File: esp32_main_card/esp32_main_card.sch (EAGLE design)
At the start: 4 parts, among them J1 09231486921, U3 ESP32-DEVKITC-32D

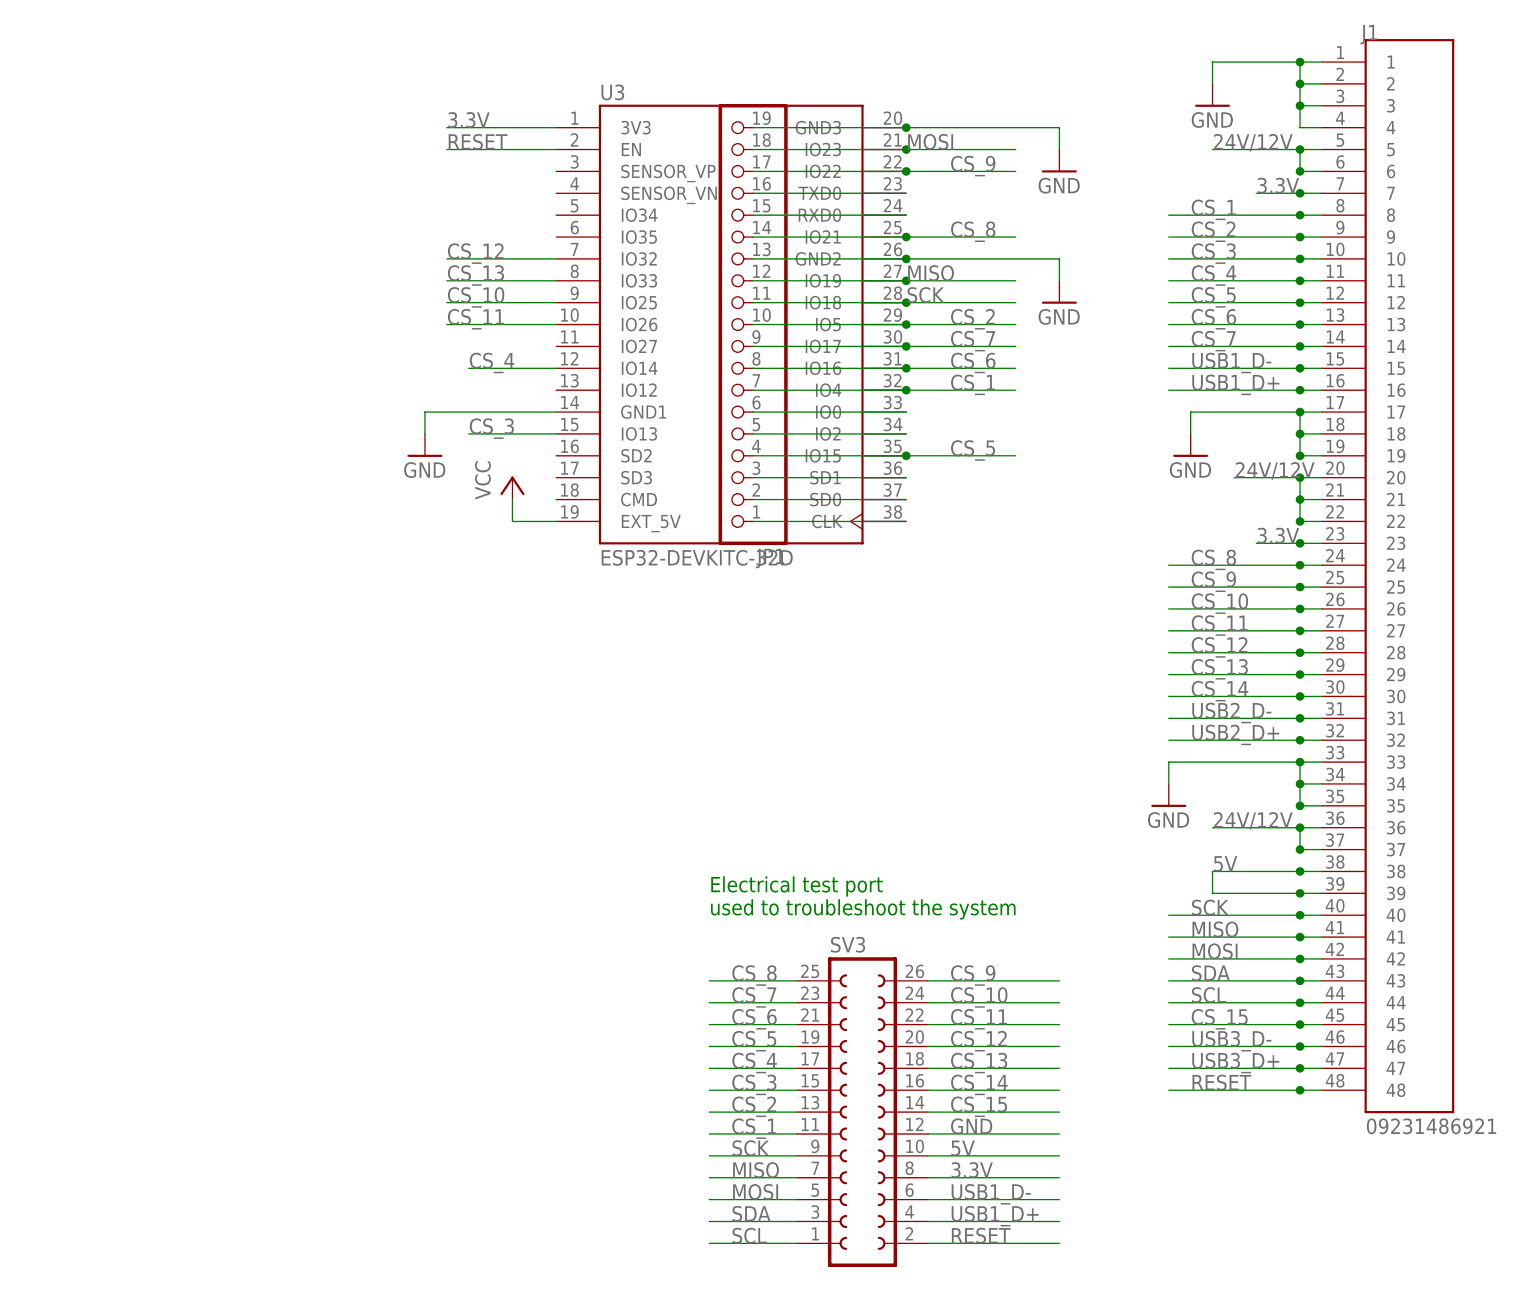
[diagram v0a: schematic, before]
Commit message: made card holes bigger, started usb port work, but I'm not done that part yet
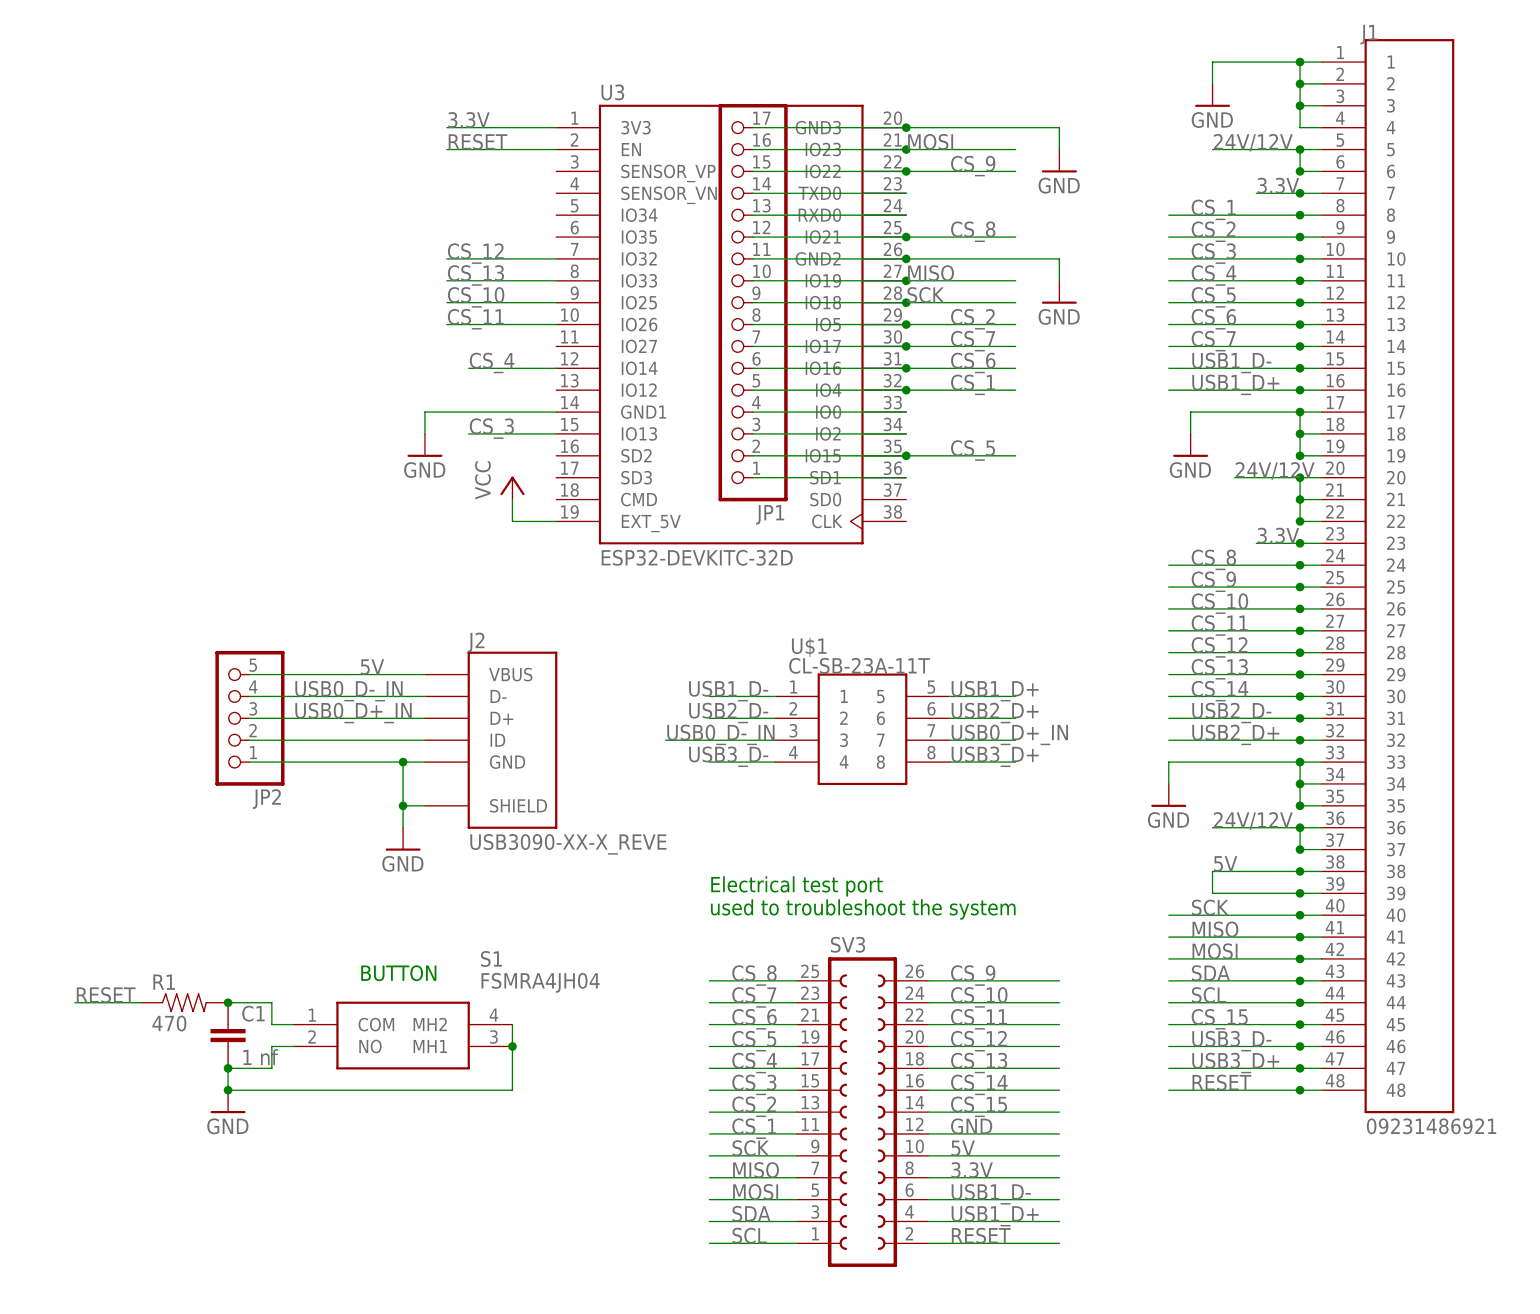
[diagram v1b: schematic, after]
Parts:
- added C1: 1 nf, SparkFun-Passives:CAP0805
- added J2: USB3090-XX-X_REVE, USB3090-XX-X_REVE:USB3090-XX-X_REVE
- added JP2: (no value), pinhead:PINHD-1X5
- added R1: 470, SparkFun-Passives:RESISTOR0805-RES
- added S1: FSMRA4JH04, FSMRA4JH04:FSMRA4JH04
- added U$1: CL-SB-23A-11T, CL-SB-23A-11T:CL-SB-23A-11T
- JP1: device pinhead:PINHD-1X19 -> pinhead:PINHD-1X17; COMPONENT female header 1x19 -> (none)
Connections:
- removed net N$9: JP1.1, U3.CLK
- new net N$1: J2.ID, JP2.2
- new net N$2: JP1.17, U3.GND3
- new net USB0_D+_IN: J2.D+, JP2.3, U$1.7
- new net USB0_D-_IN: J2.D-, JP2.4, U$1.3
- net 5V: now also J2.VBUS, JP2.5
- net CS_1: now also JP1.5; no longer JP1.7
- net CS_2: now also JP1.8; no longer JP1.10
- net CS_5: now also JP1.2; no longer JP1.4
- net CS_6: now also JP1.6; no longer JP1.8
- net CS_7: now also JP1.7; no longer JP1.9
- net CS_8: now also JP1.12; no longer JP1.14
- net CS_9: now also JP1.15; no longer JP1.17
- net GND: now also C1.2, J2.GND, J2.SHIELD, JP1.11, JP2.1, S1.MH1, S1.MH2, S1.NO; no longer JP1.13, JP1.19, U3.GND3
- net MISO: now also JP1.10; no longer JP1.12
- net MOSI: now also JP1.16; no longer JP1.18
- net N$3: now also JP1.14; no longer JP1.16
- net N$4: now also JP1.13; no longer JP1.15
- net N$5: now also JP1.4; no longer JP1.6
- net N$6: now also JP1.3; no longer JP1.5
- net N$7: now also JP1.1; no longer JP1.3
- net N$8: now also C1.1, R1.2, S1.COM; no longer JP1.2, U3.SD0
- net RESET: now also R1.1
- net SCK: now also JP1.9; no longer JP1.11
- net USB1_D+: now also U$1.5
- net USB1_D-: now also U$1.1
- net USB2_D+: now also U$1.6
- net USB2_D-: now also U$1.2
- net USB3_D+: now also U$1.8
- net USB3_D-: now also U$1.4
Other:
- note added: "BUTTON"

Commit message: added on light to main card
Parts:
- added LED1: (no value), led:LED3MM
- added R2: 180, SparkFun-Passives:RESISTOR0805-RES
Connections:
- net VCC renamed N$10
- new net N$9: LED1.C, R2.2
- net 3.3V: now also LED1.A
- net GND: now also R2.1
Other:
- note added: "ON light"
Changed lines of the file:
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@@
 <part name="GND3" library="supply1" library_urn="urn:adsk.eagle:library:371" deviceset="GND" device=""/>
 <part name="U3" library="ESP32-DEVKITC-32D" deviceset="ESP32-DEVKITC-32D" device=""/>
-<part name="P+4" library="supply1" library_urn="urn:adsk.eagle:library:371" deviceset="VCC" device=""/>
 <part name="GND9" library="supply1" library_urn="urn:adsk.eagle:library:371" deviceset="GND" device=""/>
 <part name="GND10" library="supply1" library_urn="urn:adsk.eagle:library:371" deviceset="GND" device=""/>
@@
 <part name="R1" library="SparkFun-Passives" deviceset="RESISTOR" device="0805-RES" package3d_urn="urn:adsk.eagle:package:30824479/1" value="470"/>
 <part name="GND5" library="supply1" library_urn="urn:adsk.eagle:library:371" deviceset="GND" device=""/>
+<part name="LED1" library="led" library_urn="urn:adsk.eagle:library:259" deviceset="LED" device="3MM" package3d_urn="urn:adsk.eagle:package:15797/1">
+<attribute name="COLOR" value="green"/>
+</part>
+<part name="R2" library="SparkFun-Passives" deviceset="RESISTOR" device="0805-RES" package3d_urn="urn:adsk.eagle:package:30824479/1" value="180"/>
+<part name="GND6" library="supply1" library_urn="urn:adsk.eagle:library:371" deviceset="GND" device=""/>
 </parts>
 <sheets>
@@
 used to troubleshoot the system</text>
 <text x="-55.88" y="0" size="1.778" layer="91">BUTTON</text>
+<text x="-93.98" y="63.5" size="1.778" layer="91">ON light</text>
 </plain>
 <instances>
@@
 <attribute name="VALUE" x="-27.9563" y="48.2302" size="1.7799" layer="96"/>
 </instance>
-<instance part="P+4" gate="VCC" x="-38.1" y="58.42" smashed="yes">
-<attribute name="VALUE" x="-40.64" y="55.88" size="1.778" layer="96" rot="R90"/>
-</instance>
 <instance part="GND9" gate="1" x="-48.26" y="60.96" smashed="yes">
 <attribute name="VALUE" x="-50.8" y="58.42" size="1.778" layer="96"/>
@@
 <instance part="GND5" gate="1" x="-71.12" y="-15.24" smashed="yes">
 <attribute name="VALUE" x="-73.66" y="-17.78" size="1.778" layer="96"/>
+</instance>
+<instance part="LED1" gate="G$1" x="-91.44" y="53.34" smashed="yes">
+<attribute name="NAME" x="-87.884" y="48.768" size="1.778" layer="95" rot="R90"/>
+<attribute name="VALUE" x="-85.725" y="48.768" size="1.778" layer="96" rot="R90"/>
+<attribute name="COLOR" x="-91.44" y="53.34" size="1.778" layer="96" display="off"/>
+</instance>
+<instance part="R2" gate="G$1" x="-91.44" y="43.18" smashed="yes" rot="R90">
+<attribute name="NAME" x="-92.9386" y="39.37" size="1.778" layer="95" rot="R90"/>
+<attribute name="VALUE" x="-88.138" y="39.37" size="1.778" layer="96" rot="R90"/>
+</instance>
+<instance part="GND6" gate="1" x="-91.44" y="35.56" smashed="yes">
+<attribute name="VALUE" x="-93.98" y="33.02" size="1.778" layer="96"/>
 </instance>
 </instances>
@@
 <junction x="-71.12" y="-12.7"/>
 </segment>
+<segment>
+<pinref part="R2" gate="G$1" pin="1"/>
+<pinref part="GND6" gate="1" pin="GND"/>
+</segment>
 </net>
 <net name="24V/12V" class="1">
@@
 <label x="12.7" y="-22.86" size="1.778" layer="95"/>
 </segment>
+<segment>
+<pinref part="LED1" gate="G$1" pin="A"/>
+<wire x1="-91.44" y1="55.88" x2="-91.44" y2="58.42" width="0.1524" layer="91"/>
+<wire x1="-91.44" y1="58.42" x2="-78.74" y2="58.42" width="0.1524" layer="91"/>
+<label x="-88.9" y="58.42" size="1.778" layer="95"/>
+</segment>
 </net>
 <net name="CS_1" class="0">
@@
 </segment>
 </net>
-<net name="VCC" class="0">
-<segment>
-<pinref part="U3" gate="G$1" pin="EXT_5V"/>
-<wire x1="-33.02" y1="53.34" x2="-38.1" y2="53.34" width="0.1524" layer="91"/>
-<wire x1="-38.1" y1="53.34" x2="-38.1" y2="55.88" width="0.1524" layer="91"/>
-<pinref part="P+4" gate="VCC" pin="VCC"/>
-</segment>
-</net>
 <net name="N$3" class="0">
 <segment>
@@
 </segment>
 </net>
+<net name="N$9" class="0">
+<segment>
+<pinref part="LED1" gate="G$1" pin="C"/>
+<pinref part="R2" gate="G$1" pin="2"/>
+</segment>
+</net>
+<net name="N$10" class="0">
+<segment>
+<pinref part="U3" gate="G$1" pin="EXT_5V"/>
+<wire x1="-33.02" y1="53.34" x2="-38.1" y2="53.34" width="0.1524" layer="91"/>
+</segment>
+</net>

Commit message: small mechanical changes to some cards, output connectors were moved around
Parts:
- removed R1: 470, SparkFun-Passives:RESISTOR0805-RES
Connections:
- removed net N$8: C1.1, R1.2, S1.COM
- net RESET: now also C1.1, S1.COM; no longer R1.1
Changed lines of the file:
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@@
 <part name="S1" library="FSMRA4JH04" deviceset="FSMRA4JH04" device=""/>
 <part name="C1" library="SparkFun-Passives" deviceset="CAP" device="0805" package3d_urn="urn:adsk.eagle:package:30824479/1" value="1 nf"/>
-<part name="R1" library="SparkFun-Passives" deviceset="RESISTOR" device="0805-RES" package3d_urn="urn:adsk.eagle:package:30824479/1" value="470"/>
 <part name="GND5" library="supply1" library_urn="urn:adsk.eagle:library:371" deviceset="GND" device=""/>
 <part name="LED1" library="led" library_urn="urn:adsk.eagle:library:259" deviceset="LED" device="3MM" package3d_urn="urn:adsk.eagle:package:15797/1">
@@
 <attribute name="VALUE" x="-69.596" y="-9.779" size="1.778" layer="96"/>
 </instance>
-<instance part="R1" gate="G$1" x="-76.2" y="-2.54" smashed="yes">
-<attribute name="NAME" x="-80.01" y="-1.0414" size="1.778" layer="95"/>
-<attribute name="VALUE" x="-80.01" y="-5.842" size="1.778" layer="96"/>
-</instance>
 <instance part="GND5" gate="1" x="-71.12" y="-15.24" smashed="yes">
 <attribute name="VALUE" x="-73.66" y="-17.78" size="1.778" layer="96"/>
@@
 </segment>
 <segment>
-<pinref part="R1" gate="G$1" pin="1"/>
-<wire x1="-81.28" y1="-2.54" x2="-88.9" y2="-2.54" width="0.1524" layer="91"/>
 <label x="-88.9" y="-2.54" size="1.778" layer="95"/>
+<pinref part="C1" gate="G$1" pin="1"/>
+<wire x1="-66.04" y1="-2.54" x2="-71.12" y2="-2.54" width="0.1524" layer="91"/>
+<pinref part="S1" gate="G$1" pin="COM"/>
+<wire x1="-63.5" y1="-5.08" x2="-66.04" y2="-5.08" width="0.1524" layer="91"/>
+<wire x1="-66.04" y1="-5.08" x2="-66.04" y2="-2.54" width="0.1524" layer="91"/>
+<wire x1="-88.9" y1="-2.54" x2="-71.12" y2="-2.54" width="0.1524" layer="91"/>
+<junction x="-71.12" y="-2.54"/>
 </segment>
 </net>
@@
 </segment>
 </net>
-<net name="N$8" class="0">
-<segment>
-<pinref part="C1" gate="G$1" pin="1"/>
-<wire x1="-66.04" y1="-2.54" x2="-71.12" y2="-2.54" width="0.1524" layer="91"/>
-<pinref part="S1" gate="G$1" pin="COM"/>
-<wire x1="-63.5" y1="-5.08" x2="-66.04" y2="-5.08" width="0.1524" layer="91"/>
-<wire x1="-66.04" y1="-5.08" x2="-66.04" y2="-2.54" width="0.1524" layer="91"/>
-<pinref part="R1" gate="G$1" pin="2"/>
-<junction x="-71.12" y="-2.54"/>
-</segment>
-</net>

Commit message: fixed swithc pinout on the main board
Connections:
- net USB0_D+_IN: now also U$1.6; no longer U$1.7
- net USB0_D-_IN: now also U$1.8; no longer U$1.3
- net USB1_D+: now also U$1.1; no longer U$1.5
- net USB1_D-: now also U$1.3; no longer U$1.1
- net USB2_D+: now also U$1.2; no longer U$1.6
- net USB2_D-: now also U$1.4; no longer U$1.2
- net USB3_D+: now also U$1.5; no longer U$1.8
- net USB3_D-: now also U$1.7; no longer U$1.4
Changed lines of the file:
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@@
 </segment>
 <segment>
-<pinref part="U$1" gate="G$1" pin="5"/>
-<wire x1="12.7" y1="33.02" x2="20.32" y2="33.02" width="0.1524" layer="91"/>
-<label x="12.7" y="33.02" size="1.778" layer="95"/>
+<pinref part="U$1" gate="G$1" pin="1"/>
+<wire x1="-7.62" y1="33.02" x2="-15.24" y2="33.02" width="0.1524" layer="91"/>
+<label x="-17.78" y="33.02" size="1.778" layer="95"/>
 </segment>
 </net>
@@
 </segment>
 <segment>
-<pinref part="U$1" gate="G$1" pin="6"/>
-<wire x1="12.7" y1="30.48" x2="20.32" y2="30.48" width="0.1524" layer="91"/>
-<label x="12.7" y="30.48" size="1.778" layer="95"/>
+<pinref part="U$1" gate="G$1" pin="2"/>
+<wire x1="-7.62" y1="30.48" x2="-15.24" y2="30.48" width="0.1524" layer="91"/>
+<label x="-17.78" y="30.48" size="1.778" layer="95"/>
 </segment>
 </net>
@@
 </segment>
 <segment>
-<pinref part="U$1" gate="G$1" pin="4"/>
-<wire x1="-7.62" y1="25.4" x2="-15.24" y2="25.4" width="0.1524" layer="91"/>
-<label x="-17.78" y="25.4" size="1.778" layer="95"/>
+<pinref part="U$1" gate="G$1" pin="7"/>
+<wire x1="12.7" y1="27.94" x2="20.32" y2="27.94" width="0.1524" layer="91"/>
+<label x="12.7" y="27.94" size="1.778" layer="95"/>
 </segment>
 </net>
@@
 </segment>
 <segment>
-<pinref part="U$1" gate="G$1" pin="1"/>
-<wire x1="-7.62" y1="33.02" x2="-15.24" y2="33.02" width="0.1524" layer="91"/>
-<label x="-17.78" y="33.02" size="1.778" layer="95"/>
+<pinref part="U$1" gate="G$1" pin="3"/>
+<wire x1="-7.62" y1="27.94" x2="-15.24" y2="27.94" width="0.1524" layer="91"/>
+<label x="-17.78" y="27.94" size="1.778" layer="95"/>
 </segment>
 </net>
@@
 </segment>
 <segment>
-<pinref part="U$1" gate="G$1" pin="2"/>
-<wire x1="-7.62" y1="30.48" x2="-15.24" y2="30.48" width="0.1524" layer="91"/>
-<label x="-17.78" y="30.48" size="1.778" layer="95"/>
+<pinref part="U$1" gate="G$1" pin="4"/>
+<wire x1="-7.62" y1="25.4" x2="-15.24" y2="25.4" width="0.1524" layer="91"/>
+<label x="-17.78" y="25.4" size="1.778" layer="95"/>
 </segment>
 </net>
@@
 </segment>
 <segment>
-<pinref part="U$1" gate="G$1" pin="8"/>
-<wire x1="12.7" y1="25.4" x2="20.32" y2="25.4" width="0.1524" layer="91"/>
-<label x="12.7" y="25.4" size="1.778" layer="95"/>
+<pinref part="U$1" gate="G$1" pin="5"/>
+<wire x1="12.7" y1="33.02" x2="20.32" y2="33.02" width="0.1524" layer="91"/>
+<label x="12.7" y="33.02" size="1.778" layer="95"/>
 </segment>
 </net>
@@
 </net>
 <net name="USB0_D-_IN" class="0">
-<segment>
-<pinref part="U$1" gate="G$1" pin="3"/>
-<wire x1="-7.62" y1="27.94" x2="-20.32" y2="27.94" width="0.1524" layer="91"/>
-<label x="-20.32" y="27.94" size="1.778" layer="95"/>
-</segment>
 <segment>
 <pinref part="J2" gate="G$1" pin="D-"/>
@@
 <pinref part="JP2" gate="A" pin="4"/>
 </segment>
+<segment>
+<pinref part="U$1" gate="G$1" pin="8"/>
+<wire x1="12.7" y1="25.4" x2="20.32" y2="25.4" width="0.1524" layer="91"/>
+<label x="12.7" y="25.4" size="1.778" layer="95"/>
+</segment>
 </net>
 <net name="USB0_D+_IN" class="0">
-<segment>
-<pinref part="U$1" gate="G$1" pin="7"/>
-<wire x1="12.7" y1="27.94" x2="20.32" y2="27.94" width="0.1524" layer="91"/>
-<label x="12.7" y="27.94" size="1.778" layer="95"/>
-</segment>
 <segment>
 <pinref part="J2" gate="G$1" pin="D+"/>
@@
 <pinref part="JP2" gate="A" pin="3"/>
 </segment>
-</net>
+<segment>
+<pinref part="U$1" gate="G$1" pin="6"/>
+<wire x1="12.7" y1="30.48" x2="20.32" y2="30.48" width="0.1524" layer="91"/>
+<label x="12.7" y="30.48" size="1.778" layer="95"/>
+</segment>
+</net>
